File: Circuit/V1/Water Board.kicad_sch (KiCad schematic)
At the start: 26 parts, among them J1 Pump Header, J2 Tank 1 Header, J3 Tank 2 Header, J4 Water Temp Header, J5 Water Level Header, J6 Water Level Voltage Selector, J7 Barrel_Jack, Q1 AO3400A, Q2 AO3400A, Q3 AO3400A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

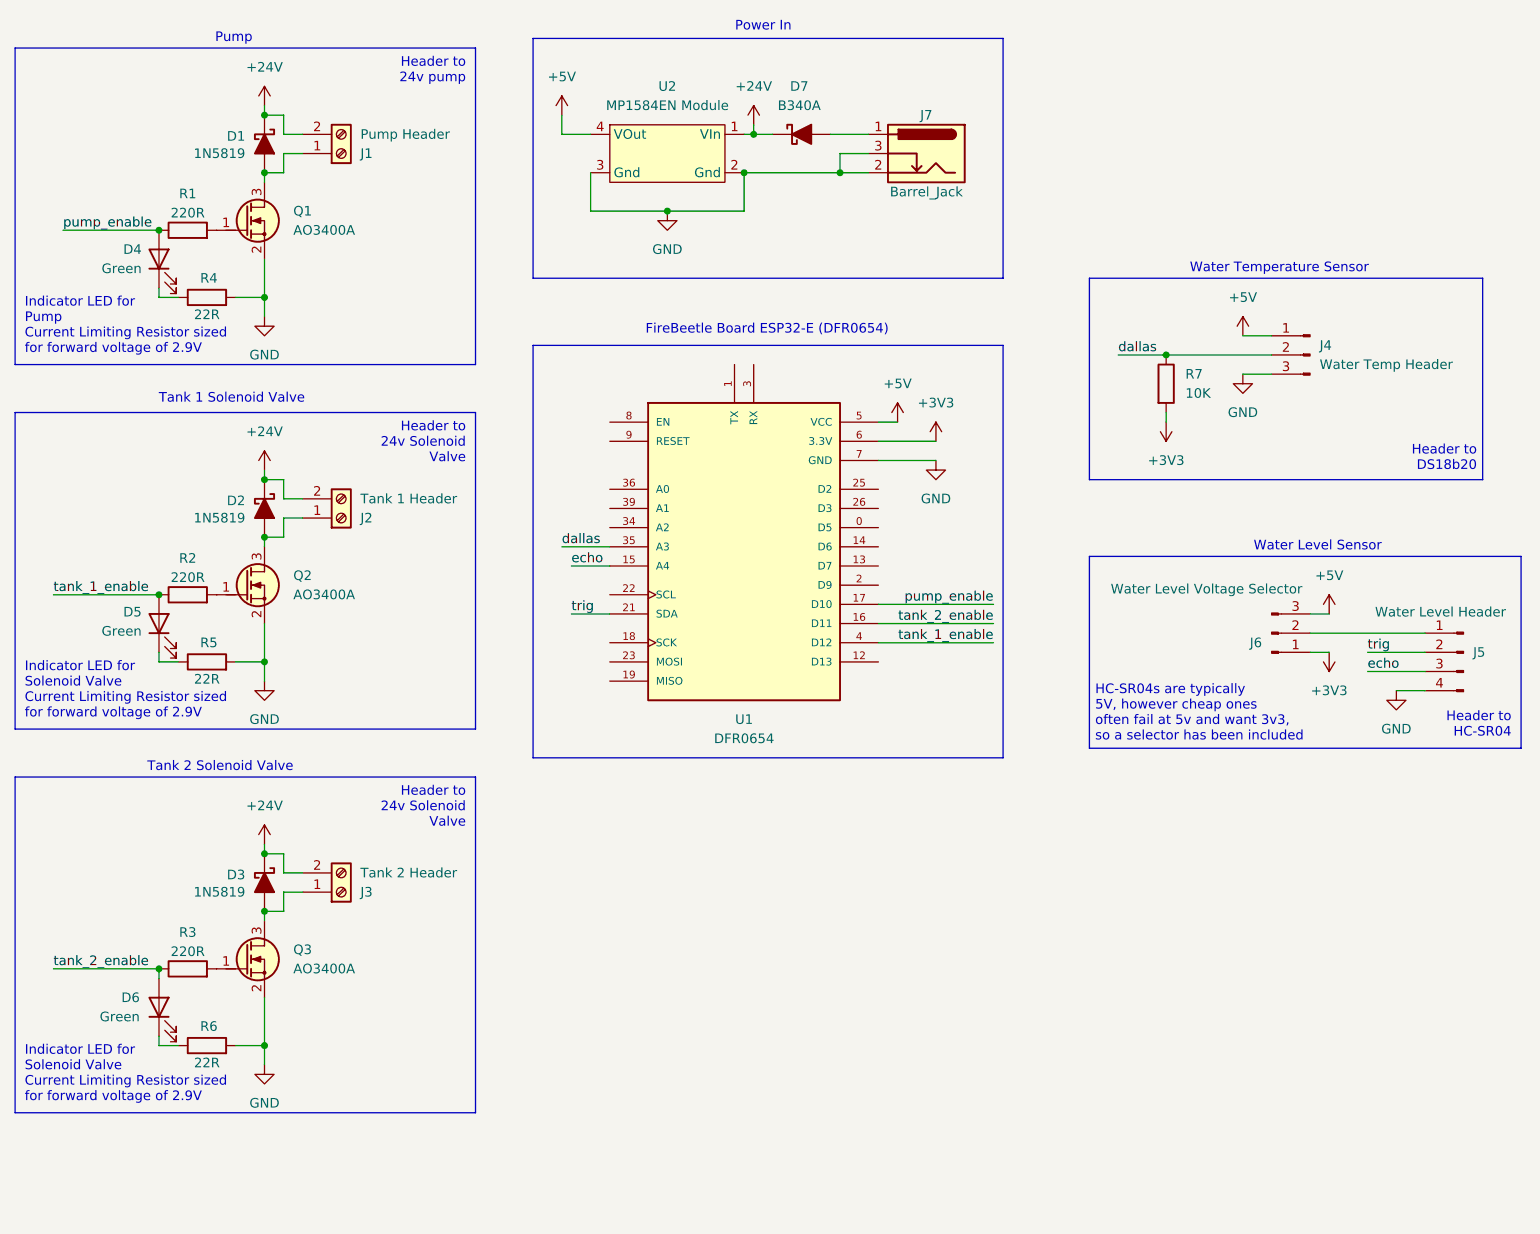
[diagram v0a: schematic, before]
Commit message: Added pull down resistors to mosfets
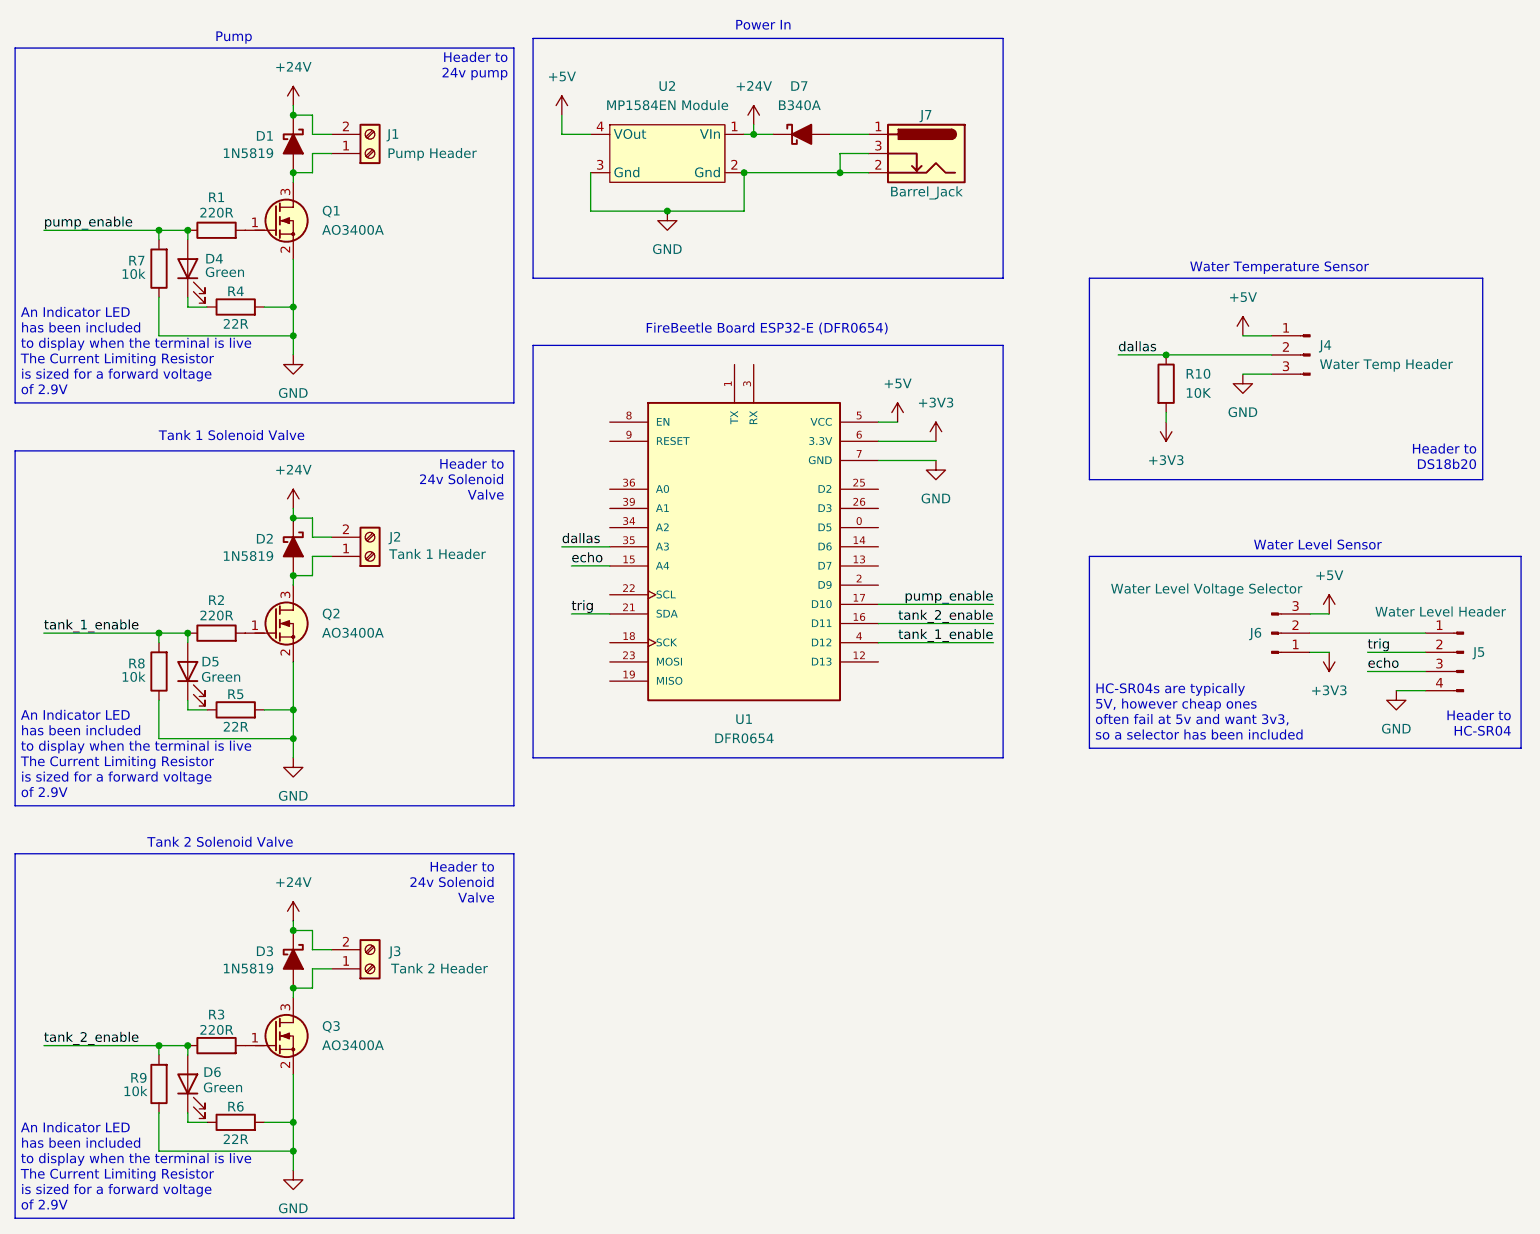
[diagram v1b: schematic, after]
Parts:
- added R7, R8, R9: 10k, Resistor_SMD:R_0805_2012Metric_Pad1.20x1.40mm_HandSolder, symbol Device:R
- D7: footprint PCM_Diode_SMD_AKL:D_SMA -> PCM_Diode_SMD_Handsoldering_AKL:D_SMA_BigPads
- Q1, Q2, Q3: footprint PCM_Package_TO_SOT_SMD_AKL:SOT-23 -> PCM_Package_TO_SOT_SMD_AKL:SOT-23_BigPads
- renumbered R7 to R10
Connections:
- net GND: now also R7.1, R8.1, R9.1
- net pump_enable: now also R7.2
- net tank_1_enable: now also R8.2
- net tank_2_enable: now also R9.2
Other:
- note added: "An Indicator LED has been included to display when the terminal is live The Current Limiting Resistor is sized for a forward voltage of 2.9V"
- note removed: "Indicator LED for Pump Current Limiting Resistor sized for forward voltage of 2.9V"
- note removed: "Indicator LED for Solenoid Valve Current Limiting Resistor sized for forward voltage of 2.9V"
- moved on the sheet: D1, D2, D3, D4, D5, D6, J1, J2, J3, Q1, Q2, Q3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
